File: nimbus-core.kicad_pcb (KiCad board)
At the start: 4 copper layers, 61.9 x 61.9 mm, 64 parts, among them J1 QTE-020-03-L-D-A, J2 QSE-020-01-L-D-A, J3 532614006, J4 USB4105-GF-A-120, J5 532614006, J6 532614006, U1 STM32F405VGT7, U2 SN65HVD233-Q1, U3 SN65HVD1782-Q1, U4 USBLC6-2P6, U5 Yellow, Y1 25MHz

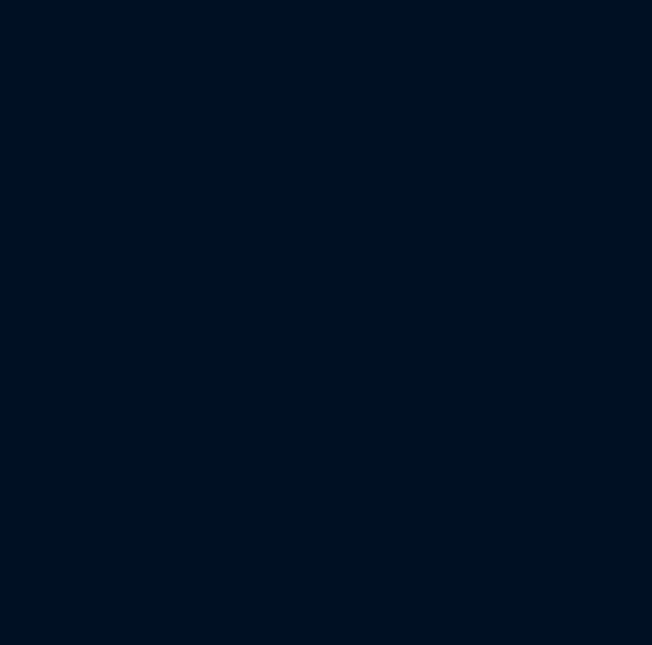
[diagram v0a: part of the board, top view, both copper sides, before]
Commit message: Update schematic symbols using the "ic" library reference to "integrated_semiconductor"
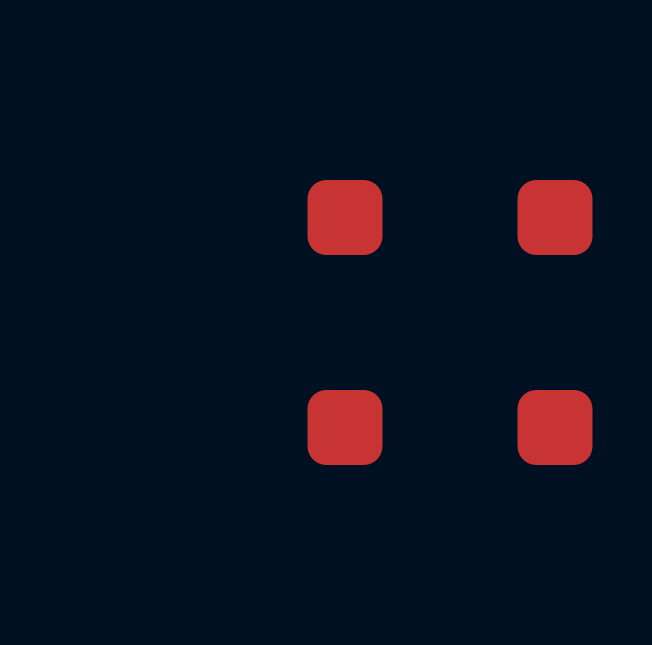
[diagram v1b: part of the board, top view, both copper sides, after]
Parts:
- added U6: ~, passive:CMT-8504-100-SMT-TR, F.Cu at (201.2, 98.5)

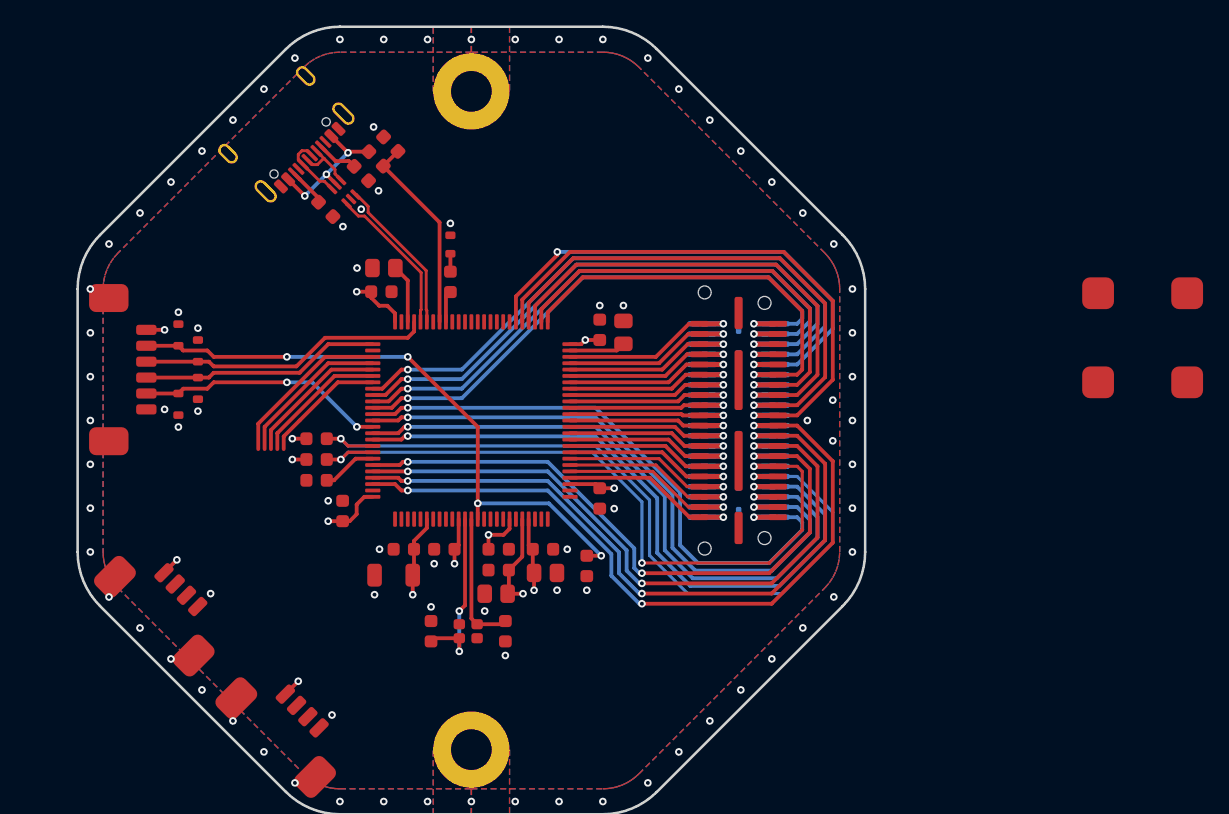
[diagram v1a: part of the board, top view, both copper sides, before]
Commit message: Remove 6 GPIOs to add VBAT, +5V, +3.3V power rails in the passthrough connector
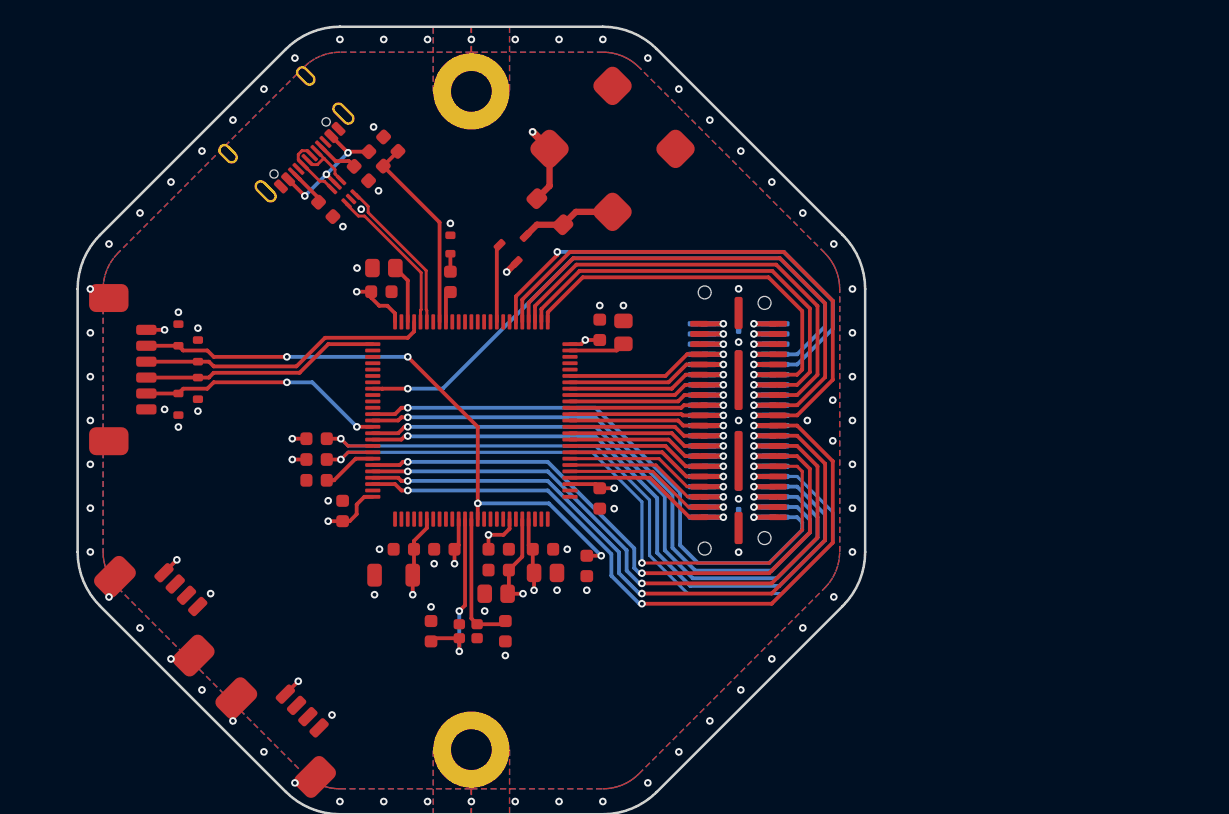
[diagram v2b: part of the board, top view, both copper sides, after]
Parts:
- added D5: ~, diode:S07M-GS18, F.Cu at (154.7, 88.6)
- added Q1: ~, discrete_semiconductor:MMBT2222ALT1G, F.Cu at (152.1, 91.2)
- U1: footprint ic:STM32F405VGT7 -> integrated_semiconductor:STM32F405VGT7
- U2: footprint ic:SN65HVD233-Q1 -> integrated_semiconductor:SN65HVD233-Q1
- U3: footprint ic:SN65HVD1782-Q1 -> integrated_semiconductor:SN65HVD1782-Q1
- moved U6 44.2 mm to (159.6, 83.7), turned to 45 degrees
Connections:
- J1 pad 1: /PD5 -> VBAT
- J1 pad 2: /PB11 -> VBAT
- J1 pad 3: /PD4 -> +3.3V
- J1 pad 4: /PB10 -> +3.3V
- J1 pad 5: /PD3 -> +5V
- J1 pad 6: /PE15 -> +5V
- J2 pad 1: /PD5 -> VBAT
- J2 pad 2: /PB11 -> VBAT
- J2 pad 3: /PD4 -> +3.3V
- J2 pad 4: /PB10 -> +3.3V
- J2 pad 5: /PD3 -> +5V
- J2 pad 6: /PE15 -> +5V
- U1 pad 59: /PD12 -> /BUZZER
- U1 pad 77: /BUZZER -> /PA15
- U6 pad -: unconnected-(U6-Pad-) -> Net-(Q1-C)
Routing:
- net /PD3: track 49.5 -> 0.00 mm, vias 2 -> 0
- net /PD4: track 47.5 -> 0.00 mm, vias 2 -> 0
- net /PD5: track 45.5 -> 0.00 mm, vias 2 -> 0
- net /PB11: track 14.8 -> 0.00 mm, vias 1 -> 0
- net /PB10: track 14.7 -> 0.00 mm, vias 1 -> 0
- net /PE15: track 14.5 -> 0.00 mm, vias 1 -> 0
- net +3.3V: track 49.1 -> 62.8 mm, vias 14 -> 17
- net /USART3_TX: track 13.2 -> 0.00 mm
- net /USART3_RX: track 12.3 -> 0.00 mm
- net /RS-485_DIR: track 11.5 -> 0.00 mm
- net /CAN1_RX: track 10.6 -> 0.00 mm
- net /CAN1_TX: track 9.76 -> 0.00 mm
- net Net-(Q1-C): track 0.00 -> 7.61 mm
- net +5V: track 0.00 -> 7.10 mm, vias 0 -> 2
- net VBAT: track 0.00 -> 7.10 mm, vias 0 -> 2
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
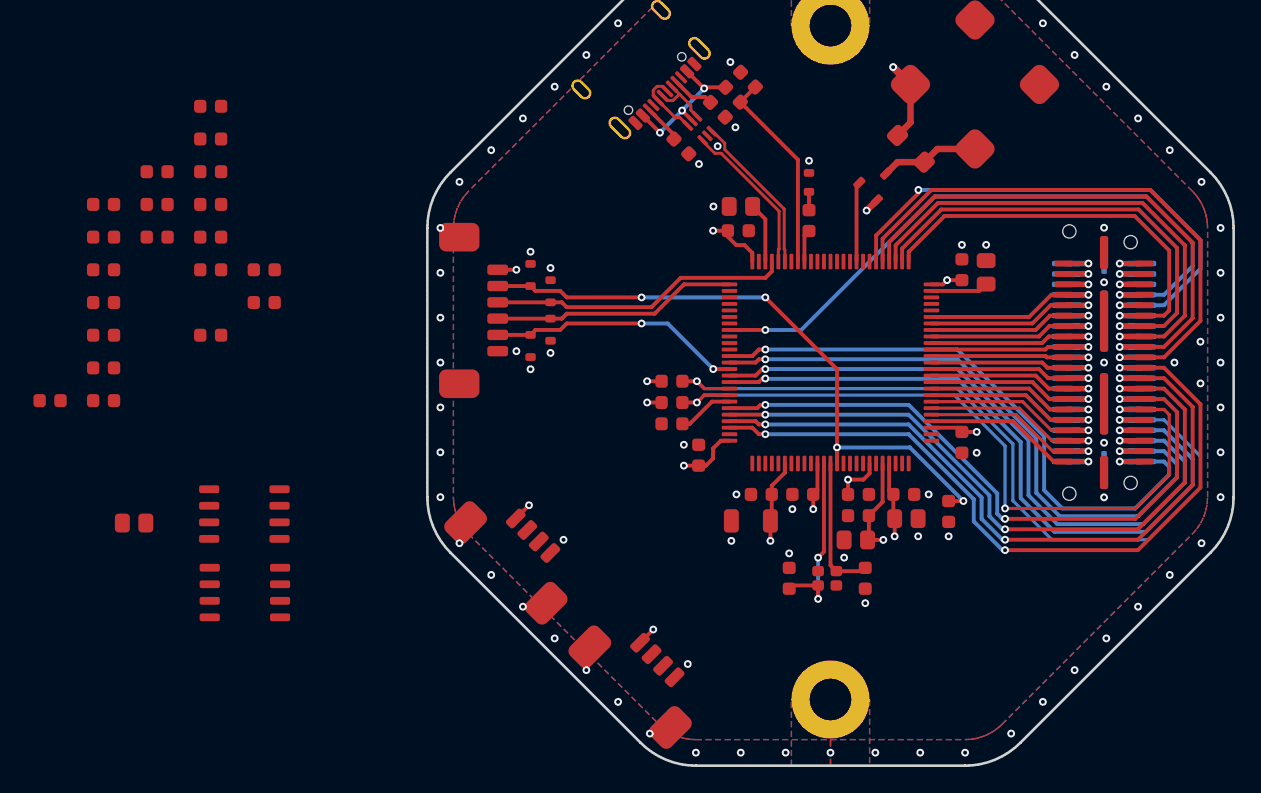
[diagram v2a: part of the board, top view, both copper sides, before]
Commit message: Added RGB LED
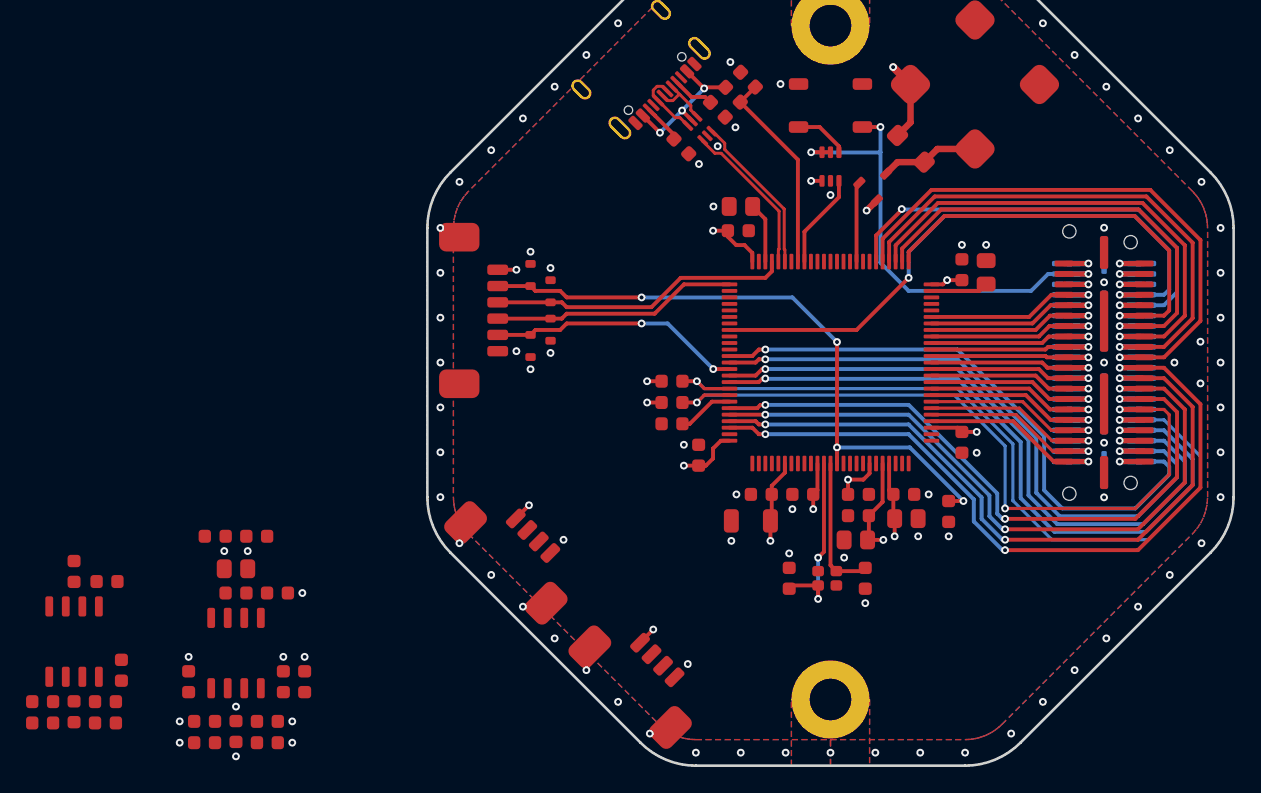
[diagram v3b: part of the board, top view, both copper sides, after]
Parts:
- removed R14: 100Ω, passive:R_0603_Density_Nominal
- added U7: ~, integrated_semiconductor:WS2812B, F.Cu at (148.5, 85.3)
- U5: value Yellow -> ~; footprint diode:TLMY1100-GS15 -> integrated_semiconductor:TXU0101DCKR
- moved R5 44.5 mm to (106.5, 129.5), turned to -90 degrees
- moved R6 41.7 mm to (99.2, 129.5), turned to -90 degrees
- moved R8 41.5 mm to (105.3, 134.2)
- moved C20 40.4 mm to (100.5, 132.5), turned to 180 degrees
- moved R7 39.8 mm to (108.1, 129.5), turned to 90 degrees
- moved C21 39.2 mm to (105.3, 132.5)
- moved R9 38.8 mm to (100.5, 134.2)
- moved C22 36.9 mm to (102.9, 133.3), turned to 90 degrees
- moved R19 36.9 mm to (92.8, 132.7)
- moved R20 36.5 mm to (88.0, 132.7)
- moved R4 28.8 mm to (106.0, 122.7), turned to 180 degrees
- moved C24 28.5 mm to (88.0, 131.0), turned to 180 degrees
- moved R2 28.3 mm to (101.3, 118.3), turned to 180 degrees
- moved C23 28.3 mm to (94.1, 128.6), turned to 90 degrees
- moved R3 26.6 mm to (104.5, 118.3)
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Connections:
- J1 pad 3: +3.3V -> +5V
- J1 pad 4: +3.3V -> +5V
- J1 pad 5: +5V -> +3.3V
- J1 pad 6: +5V -> +3.3V
- J2 pad 3: +3.3V -> +5V
- J2 pad 4: +3.3V -> +5V
- J2 pad 5: +5V -> +3.3V
- J2 pad 6: +5V -> +3.3V
- U5 pad 1: GND -> +3.3V
- U5 pad 2: Net-(R14-Pad2) -> GND
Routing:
- net +5V: track 7.10 -> 41.4 mm, vias 2 -> 4
- net /STATUS_LED: track 2.49 -> 7.29 mm
- net /PD9: track 41.5 -> 37.3 mm
- net Net-(U5-BY): track 0.00 -> 4.17 mm
- net /PD2: track 51.5 -> 48.5 mm
- net Net-(R14-Pad2): track 1.41 -> 0.00 mm
- net /~{MCU_RESET}: track 48.5 -> 49.7 mm
- net +3.3V: track 62.8 -> 63.7 mm, vias 17 -> 21
- net Net-(C22-Pad1): vias 0 -> 3
- net GND: vias 35 -> 42

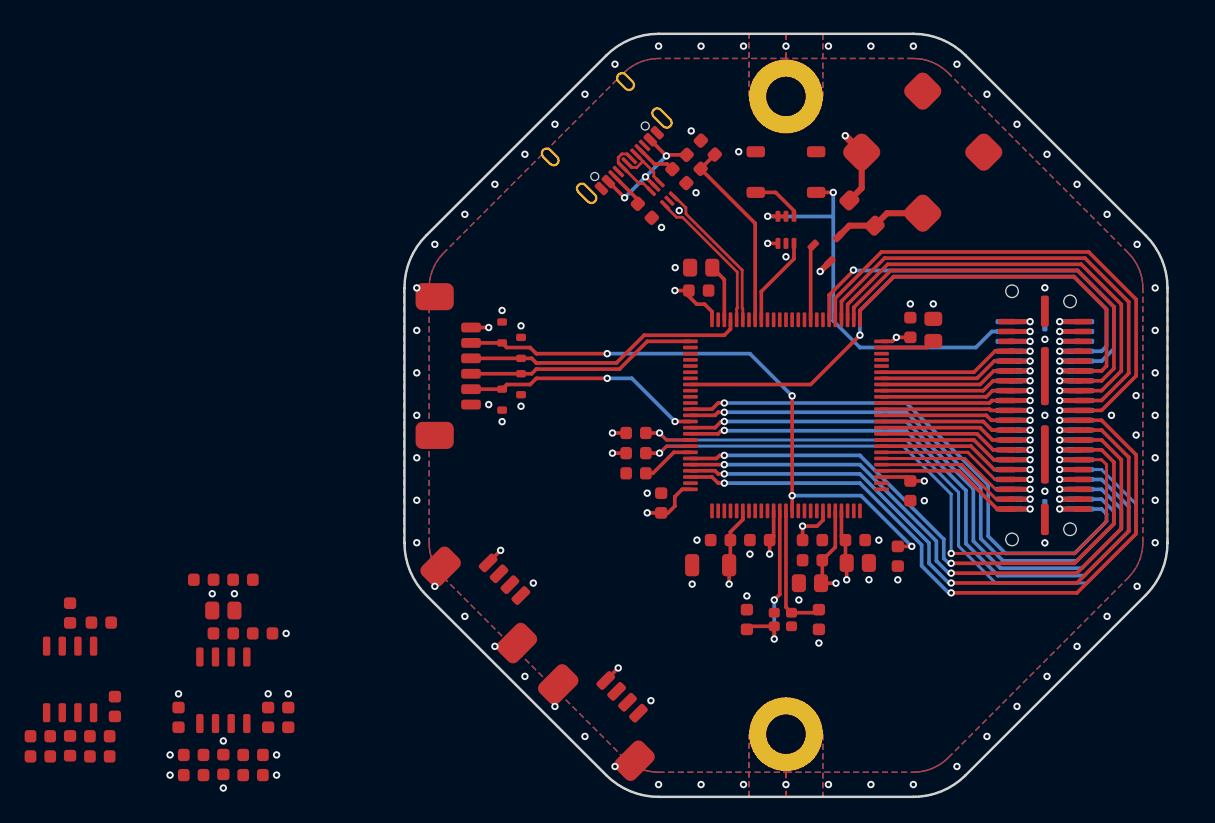
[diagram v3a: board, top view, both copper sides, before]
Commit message: Add reset tactile switch, CAN routing and BOOT0 SPDT switch
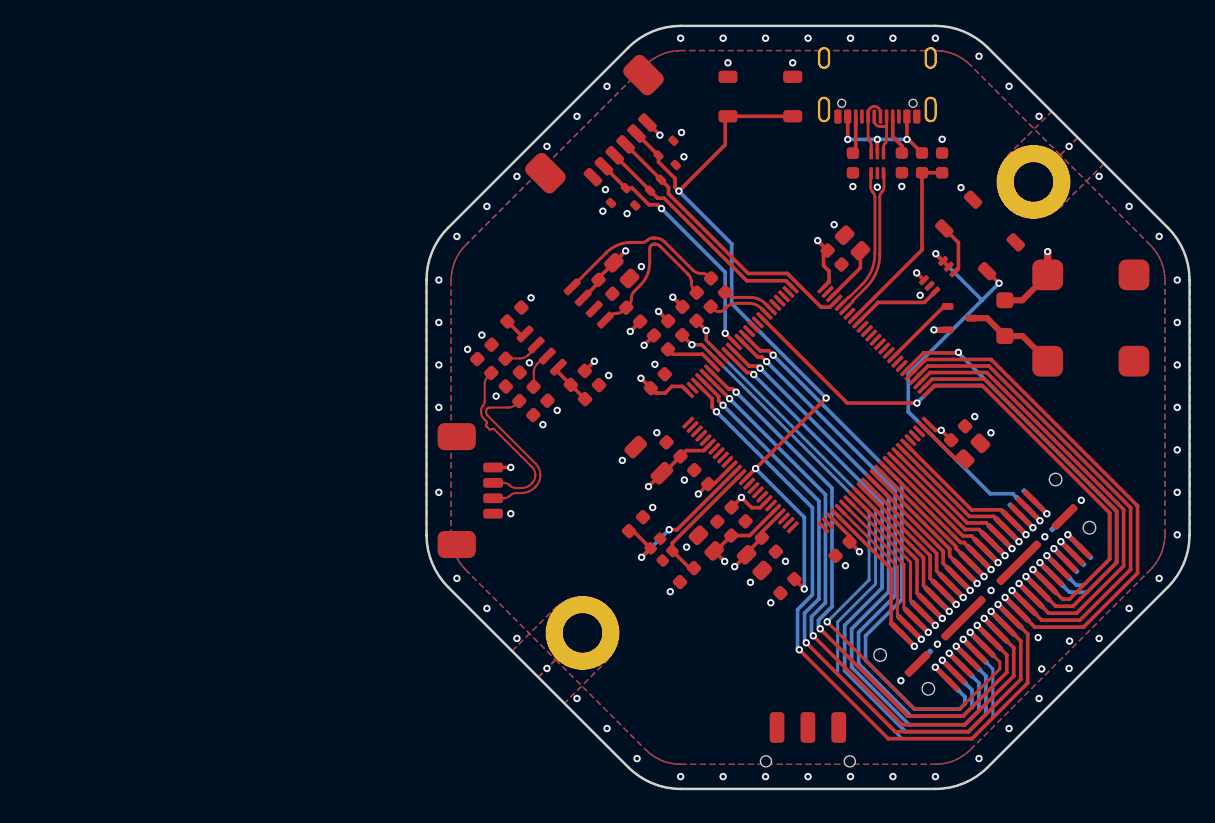
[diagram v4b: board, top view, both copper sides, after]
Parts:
- removed C23, C24, C25: 100nF, passive:C_0603_Density_Nominal
- removed C26: 4.7nF, passive:C_0603_Density_Nominal
- removed J6: 532614006, connector:532614004
- removed the R10 at (93.0, 121.8)
- removed the R11 at (90.4, 121.0)
- removed R19, R20: 60.4Ω, passive:R_0603_Density_Nominal
- removed the U3 at (90.4, 126.4)
- added SW1: ~, electromechanical:PTS647SN50SMTR2 LFS, F.Cu at (146.4, 79.1)
- added SW2: ~, electromechanical:JS102011SAQN, F.Cu at (150.3, 133.1)
- J1: value QTE-020-03-L-D-A -> Val**
- J2: value QSE-020-01-L-D-A -> Val**
- U1: value STM32F405VGT7 -> LQFP100
- U3: renamed from U2; value SN65HVD233-Q1 -> SOIC-8
- U5: renamed from U4; value USBLC6-2P6 -> SOT-666-6
- moved R2 48.1 mm to (143.0, 94.5), turned to 135 degrees
- moved R3 43.7 mm to (141.8, 95.6), turned to 135 degrees
- moved R6 42.5 mm to (126.5, 96.8), turned to -135 degrees
- moved C12 42.5 mm to (135.2, 93.3), turned to -45 degrees
- moved C15 41.8 mm to (133.9, 94.6), turned to -45 degrees
- moved C20 41.0 mm to (125.2, 99.8), turned to 135 degrees
- moved R9 40.7 mm to (124.0, 101.0), turned to -45 degrees
- moved U3 40.5 mm to (130.6, 97.8), turned to -135 degrees
- moved R4 39.7 mm to (136.1, 96.8), turned to 135 degrees
- moved C22 39.1 mm to (126.3, 102.1), turned to 45 degrees
- moved C21 37.4 mm to (128.6, 103.2), turned to -45 degrees
- moved R5 37.3 mm to (131.6, 102.0), turned to -135 degrees
- moved R8 37.1 mm to (127.4, 104.4), turned to -45 degrees
- moved R7 36.1 mm to (132.8, 103.1), turned to 45 degrees
- moved J5 23.0 mm to (133.4, 81.8), turned to 45 degrees
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- renumbered D5 to D1, D1 to D2, D2 to D3, D3 to D4, D4 to D5, R12 to R10, R13 to R11, R15 to R12, R16 to R13, R17 to R14, R18 to R15, U6 to U2, U5 to U4, U7 to U6
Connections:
- R1 pad 2: unconnected-(R1-Pad2) -> Net-(R1-Pad2)
- U1 pad 80: /RS-485_DIR -> /PC12
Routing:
- net /CAN_P: track 0.00 -> 17.7 mm
- net /CAN_N: track 0.00 -> 17.6 mm
- net Net-(U3-RXD): track 0.00 -> 13.9 mm
- net Net-(U3-TXD): track 0.00 -> 13.4 mm
- net /~{MCU_RESET}: track 49.7 -> 62.7 mm
- net +3.3V: track 63.7 -> 69.7 mm
- net /CAN1_TX: track 0.00 -> 5.15 mm
- net /CAN1_RX: track 0.00 -> 4.19 mm
- net Net-(U3-RS): track 0.00 -> 3.66 mm
- net Net-(U3-LBK): track 0.00 -> 2.03 mm
- net Net-(R1-Pad2): track 0.00 -> 1.13 mm, vias 0 -> 1
- net CHASSIS: vias 56 -> 53
